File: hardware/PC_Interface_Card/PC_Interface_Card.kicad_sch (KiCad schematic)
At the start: 1 part, among them U1 ESP32-S3-WROOM-1

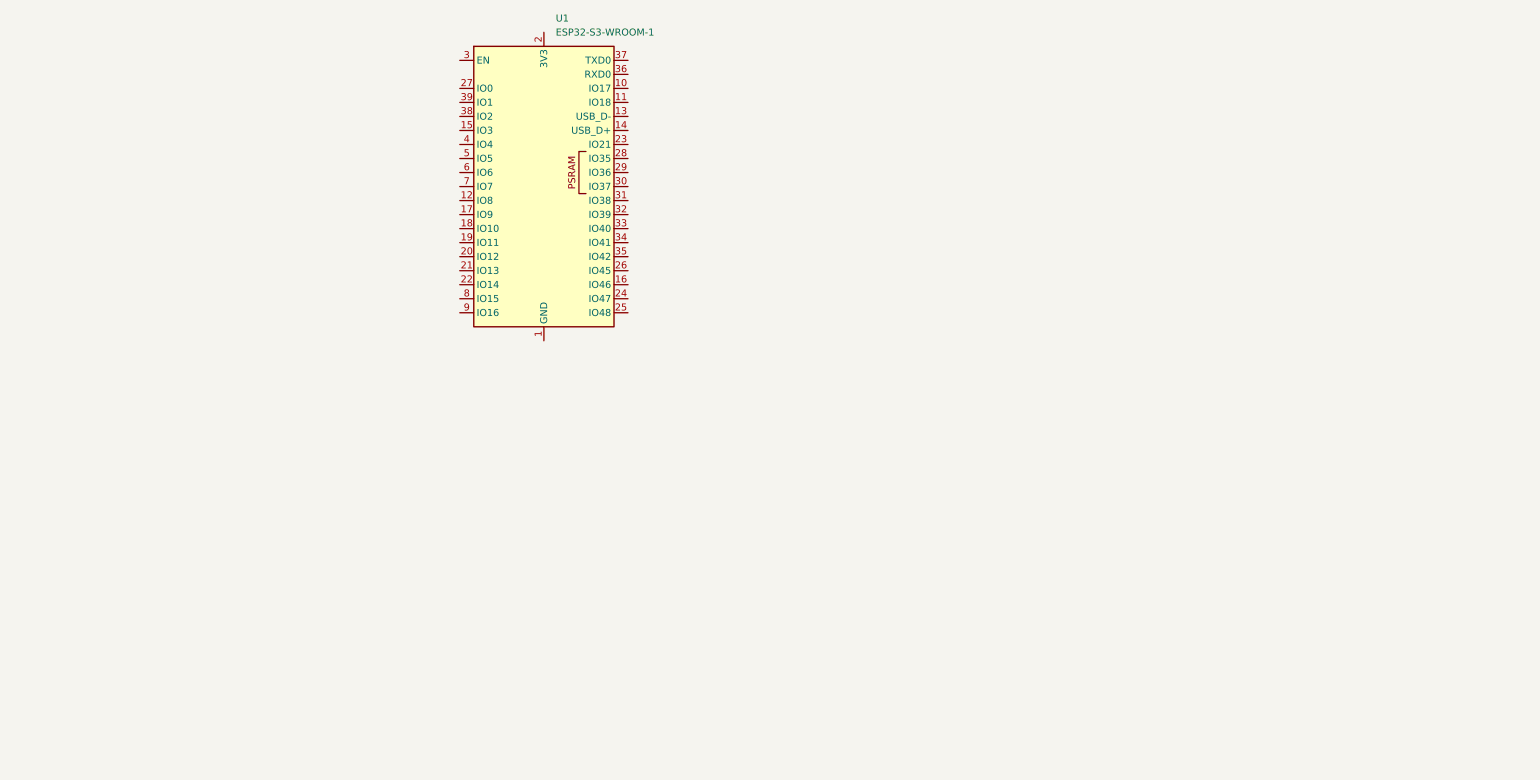
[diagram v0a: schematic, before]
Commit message: Schema additions, pending item - finalise switch
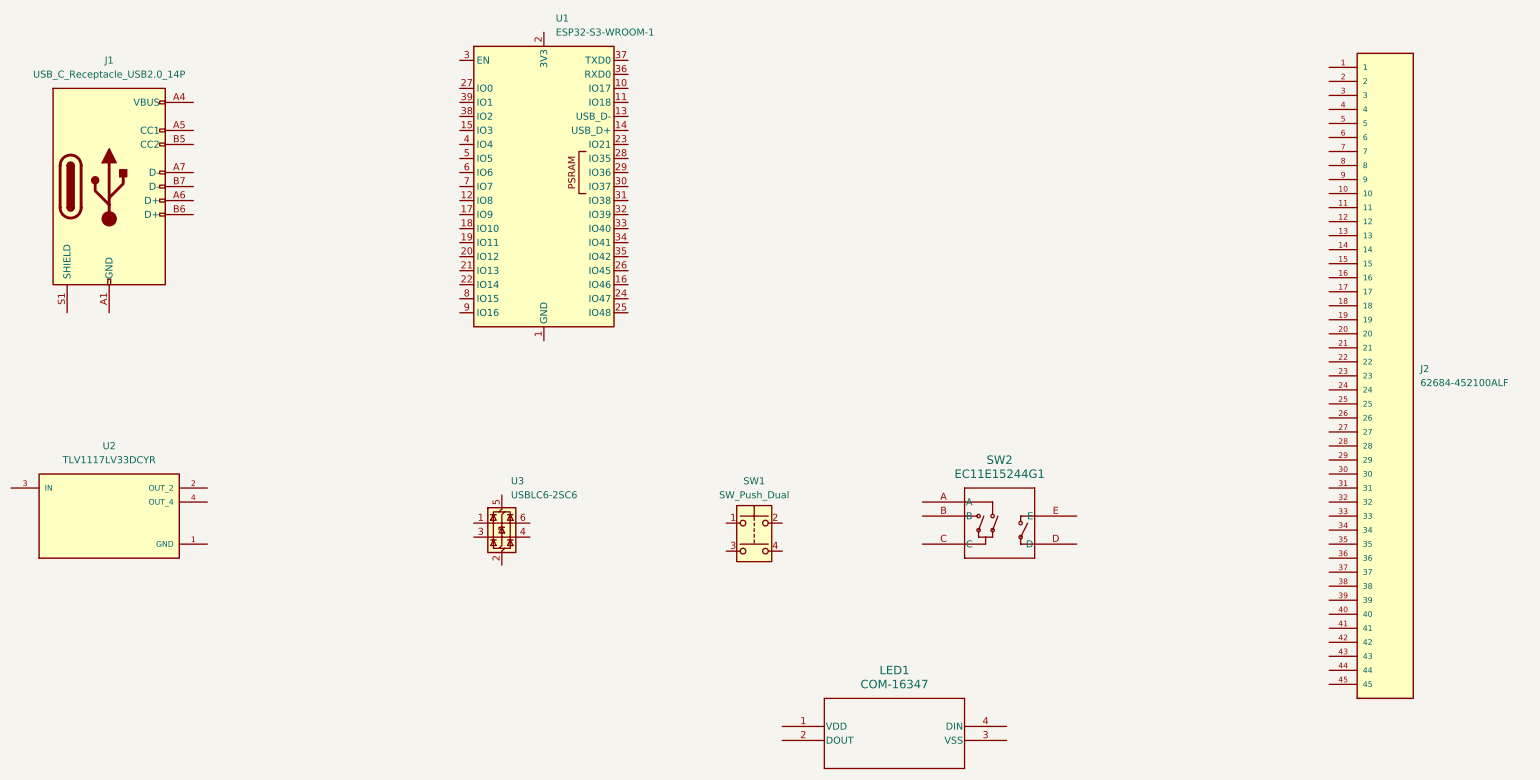
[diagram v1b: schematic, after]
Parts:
- added J1: USB_C_Receptacle_USB2.0_14P, symbol Connector:USB_C_Receptacle_USB2.0_14P
- added J2: 62684-452100ALF, 62684-452100ALF:AMPHENOL_62684-452100ALF, symbol 62684-452100ALF:62684-452100ALF
- added LED1: COM-16347, COM-16347_SPK, symbol RGB_LED_2026-01-04_20-36-32:COM-16347
- added SW1: SW_Push_Dual, symbol Switch:SW_Push_Dual
- added SW2: EC11E15244G1, EC11E15244G1_AAL, symbol Encoder_EC11E15244G1_2026-01-04_18-46-08:EC11E15244G1
- added U2: TLV1117LV33DCYR, TLV1117LV33DCYR:VREG_TLV1117LV33DCYR, symbol TLV1117LV33DCYR:TLV1117LV33DCYR
- added U3: USBLC6-2SC6, Package_TO_SOT_SMD:SOT-23-6, symbol Power_Protection:USBLC6-2SC6
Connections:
- new net: J1.A1 (GND), J1.A12 (GND), J1.B1 (GND), J1.B12 (GND)
- new net: J1.A4 (VBUS), J1.A9 (VBUS), J1.B4 (VBUS), J1.B9 (VBUS)

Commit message: Symbols and footprint added
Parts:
- removed J1: USB_C_Receptacle_USB2.0_14P, symbol Connector:USB_C_Receptacle_USB2.0_14P
- removed J2: 62684-452100ALF, 62684-452100ALF:AMPHENOL_62684-452100ALF, symbol 62684-452100ALF:62684-452100ALF
- removed LED1: COM-16347, COM-16347_SPK, symbol RGB_LED_2026-01-04_20-36-32:COM-16347
- removed SW1: SW_Push_Dual, symbol Switch:SW_Push_Dual
- removed SW2: EC11E15244G1, EC11E15244G1_AAL, symbol Encoder_EC11E15244G1_2026-01-04_18-46-08:EC11E15244G1
- removed U1: ESP32-S3-WROOM-1, RF_Module:ESP32-S3-WROOM-1, symbol RF_Module:ESP32-S3-WROOM-1
- removed U2: TLV1117LV33DCYR, TLV1117LV33DCYR:VREG_TLV1117LV33DCYR, symbol TLV1117LV33DCYR:TLV1117LV33DCYR
- removed U3: USBLC6-2SC6, Package_TO_SOT_SMD:SOT-23-6, symbol Power_Protection:USBLC6-2SC6
